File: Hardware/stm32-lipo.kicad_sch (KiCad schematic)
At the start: 48 parts, among them CN1 B2B-PH-K-S(LF)(SN), Q1 AO3401A, U1 STM32G070RBT6, U2 AMS1117, U3 826629-3, U4 826629-3, U5 BQ27441DRZR-G1A, Y1 Crystal_GND24

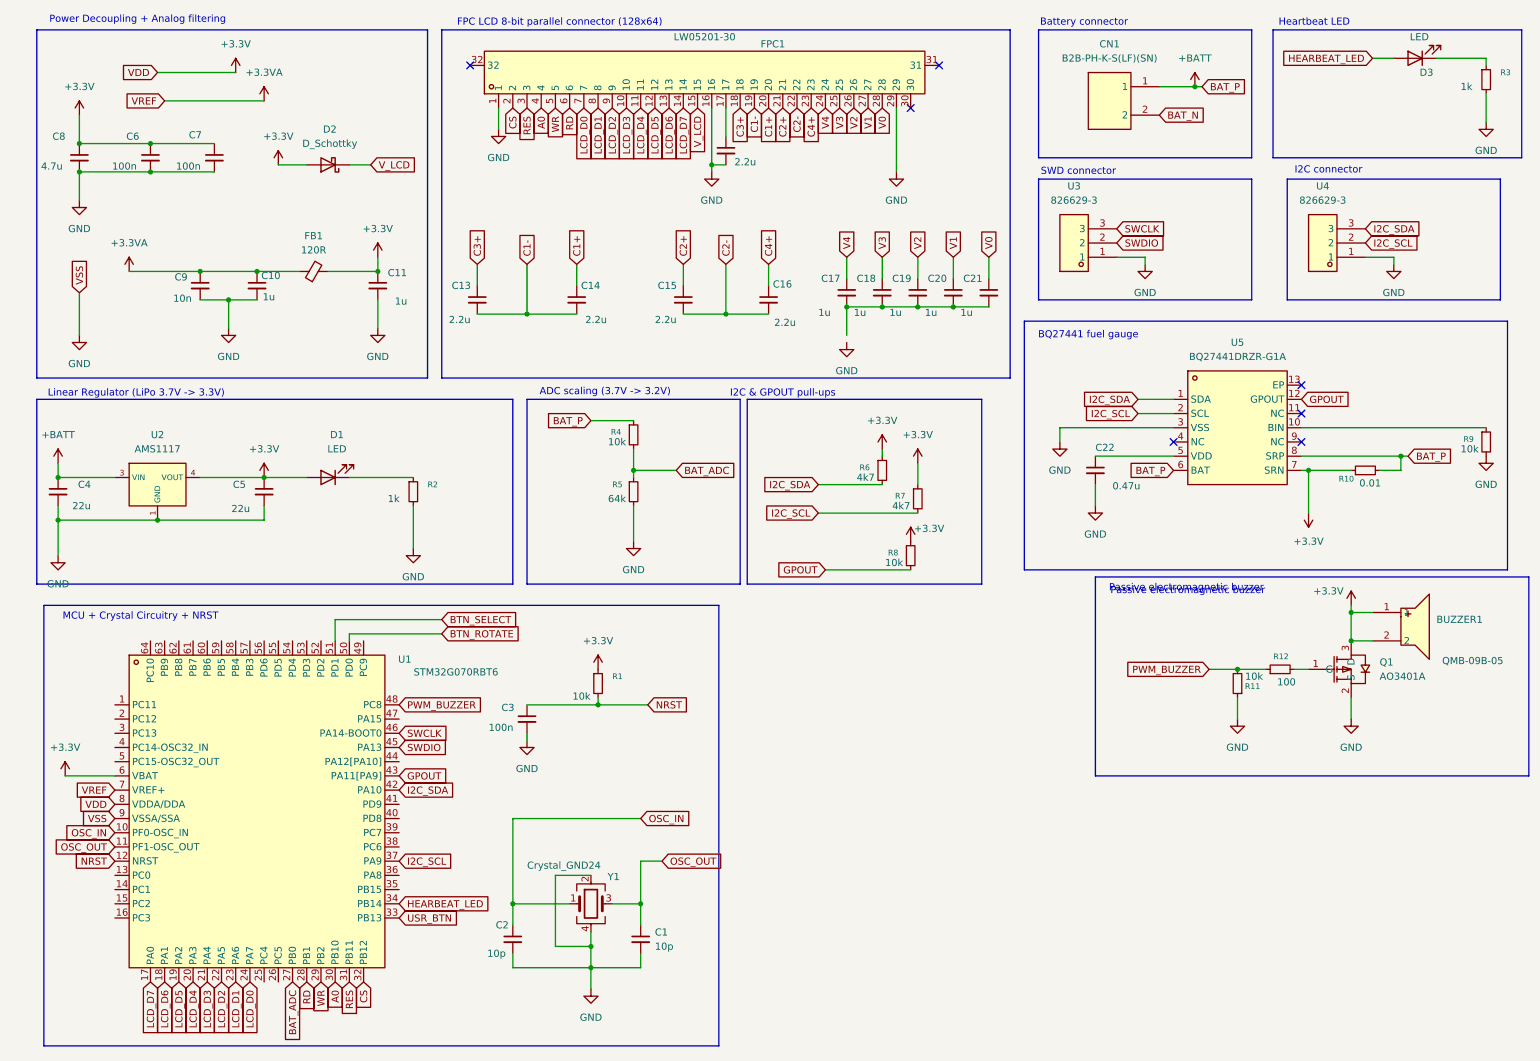
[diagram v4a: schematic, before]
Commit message: Footprint for switch, next up: replace linear regulator with buck converter, more efficient
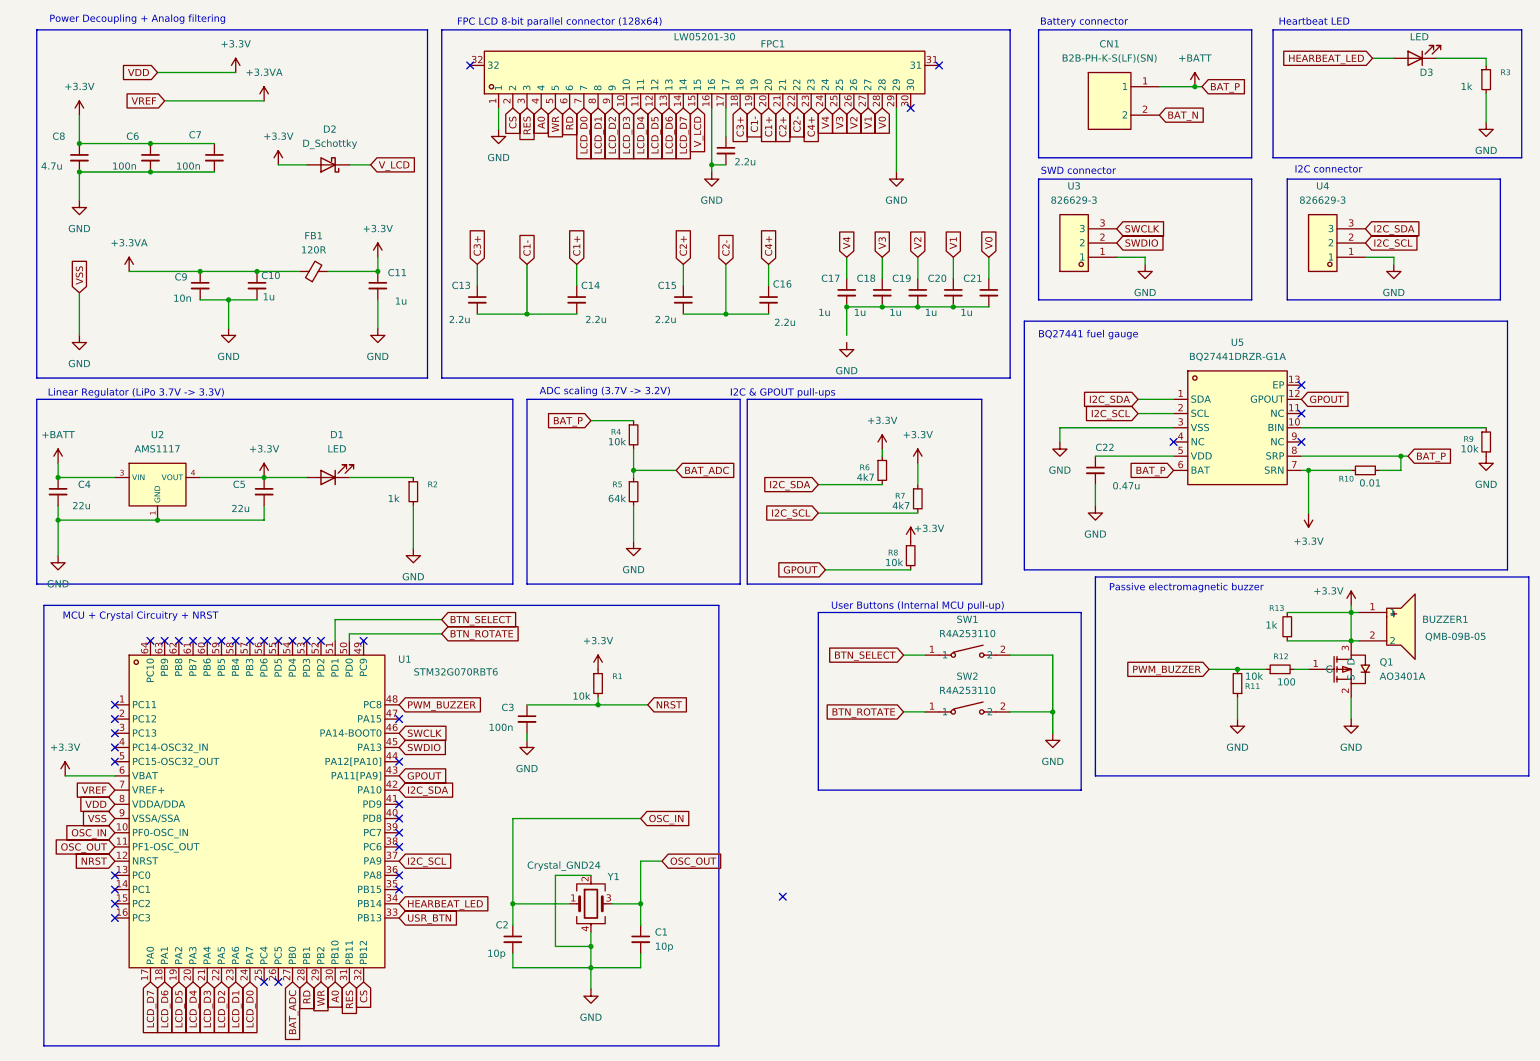
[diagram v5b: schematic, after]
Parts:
- added R13: 1k, symbol Device:R_Small
- added SW1, SW2: R4A253110, easyeda2kicad:SW-SMD_L6.2-W3.7-LS8.0, symbol easyeda2kicad:R4A253110
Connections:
- net +3.3V: now also R13.1, R13.2
- net BTN_ROTATE: now also SW2.1
- net BTN_SELECT: now also SW1.1
- net GND: now also SW1.2, SW2.2
- no-connect marks 7 -> 41
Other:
- note added: "User Buttons (Internal MCU pull-up)"
- moved on the sheet: BUZZER1
